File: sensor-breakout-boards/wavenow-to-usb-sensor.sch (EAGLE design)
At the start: 4 parts, among them X1 Type-A Receptacle, X2 Micro Type-B Receptacle

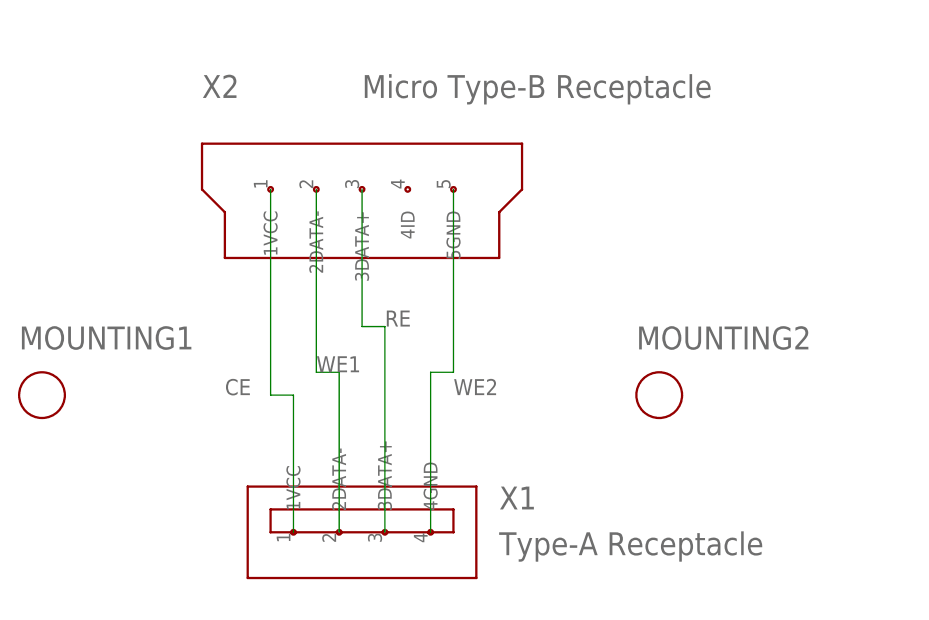
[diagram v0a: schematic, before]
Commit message: three breakout boards complete
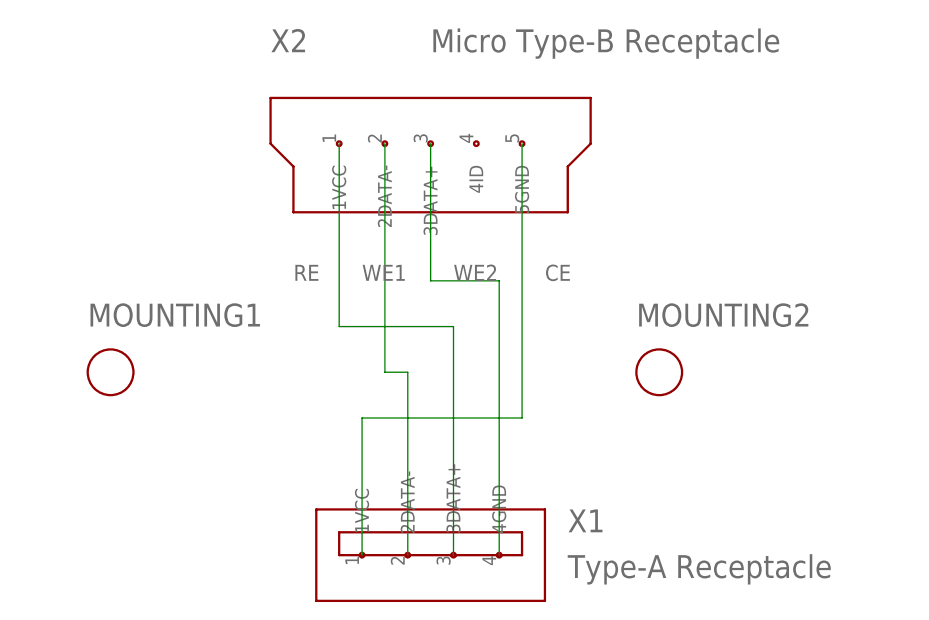
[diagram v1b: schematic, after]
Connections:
- net CE: now also X2.5GND; no longer X2.1VCC
- net RE: now also X2.1VCC; no longer X2.3DATA+
- net WE2: now also X2.3DATA+; no longer X2.5GND
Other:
- moved on the sheet: MOUNTING1, MOUNTING2, X1, X2
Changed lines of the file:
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@@
 </classes>
 <parts>
+<part name="X2" library="sensor-breakout-boards" deviceset="USB-MICRO-TYPE-B-RECEPTACLE" device="" value="Micro Type-B Receptacle"/>
 <part name="X1" library="sensor-breakout-boards" deviceset="USB-TYPE-A-RECEPTACLE" device="" value="Type-A Receptacle"/>
-<part name="X2" library="sensor-breakout-boards" deviceset="USB-MICRO-TYPE-B-RECEPTACLE" device="" value="Micro Type-B Receptacle"/>
 <part name="MOUNTING1" library="sensor-breakout-boards" deviceset="M2-MOUNTING-HOLE" device=""/>
 <part name="MOUNTING2" library="sensor-breakout-boards" deviceset="M2-MOUNTING-HOLE" device=""/>
@@
 </plain>
 <instances>
-<instance part="X1" gate="G$1" x="43.18" y="17.78"/>
-<instance part="X2" gate="G$1" x="43.18" y="55.88"/>
-<instance part="MOUNTING1" gate="G$1" x="7.62" y="33.02"/>
-<instance part="MOUNTING2" gate="G$1" x="76.2" y="33.02"/>
+<instance part="X2" gate="G$1" x="50.8" y="60.96"/>
+<instance part="X1" gate="G$1" x="50.8" y="15.24"/>
+<instance part="MOUNTING1" gate="G$1" x="15.24" y="35.56"/>
+<instance part="MOUNTING2" gate="G$1" x="76.2" y="35.56"/>
 </instances>
 <busses>
 </busses>
 <nets>
-<net name="CE" class="0">
+<net name="RE" class="0">
 <segment>
-<pinref part="X1" gate="G$1" pin="1VCC"/>
-<wire x1="35.56" y1="17.78" x2="35.56" y2="33.02" width="0.1524" layer="91"/>
-<wire x1="35.56" y1="33.02" x2="33.02" y2="33.02" width="0.1524" layer="91"/>
 <pinref part="X2" gate="G$1" pin="1VCC"/>
-<wire x1="33.02" y1="33.02" x2="33.02" y2="55.88" width="0.1524" layer="91"/>
-<label x="27.94" y="33.02" size="1.778" layer="95"/>
+<wire x1="40.64" y1="60.96" x2="40.64" y2="40.64" width="0.1524" layer="91"/>
+<pinref part="X1" gate="G$1" pin="3DATA+"/>
+<wire x1="40.64" y1="40.64" x2="53.34" y2="40.64" width="0.1524" layer="91"/>
+<wire x1="53.34" y1="40.64" x2="53.34" y2="15.24" width="0.1524" layer="91"/>
+<label x="35.56" y="45.72" size="1.778" layer="95"/>
 </segment>
 </net>
@@
 <segment>
 <pinref part="X2" gate="G$1" pin="2DATA-"/>
-<wire x1="38.1" y1="55.88" x2="38.1" y2="35.56" width="0.1524" layer="91"/>
+<wire x1="45.72" y1="60.96" x2="45.72" y2="35.56" width="0.1524" layer="91"/>
 <pinref part="X1" gate="G$1" pin="2DATA-"/>
-<wire x1="38.1" y1="35.56" x2="40.64" y2="35.56" width="0.1524" layer="91"/>
-<wire x1="40.64" y1="35.56" x2="40.64" y2="17.78" width="0.1524" layer="91"/>
-<label x="38.1" y="35.56" size="1.778" layer="95"/>
-</segment>
-</net>
-<net name="RE" class="0">
-<segment>
-<pinref part="X2" gate="G$1" pin="3DATA+"/>
-<wire x1="43.18" y1="55.88" x2="43.18" y2="40.64" width="0.1524" layer="91"/>
-<pinref part="X1" gate="G$1" pin="3DATA+"/>
-<wire x1="43.18" y1="40.64" x2="45.72" y2="40.64" width="0.1524" layer="91"/>
-<wire x1="45.72" y1="40.64" x2="45.72" y2="17.78" width="0.1524" layer="91"/>
-<label x="45.72" y="40.64" size="1.778" layer="95"/>
+<wire x1="45.72" y1="35.56" x2="48.26" y2="35.56" width="0.1524" layer="91"/>
+<wire x1="48.26" y1="35.56" x2="48.26" y2="15.24" width="0.1524" layer="91"/>
+<label x="43.18" y="45.72" size="1.778" layer="95"/>
 </segment>
 </net>
 <net name="WE2" class="0">
 <segment>
-<pinref part="X2" gate="G$1" pin="5GND"/>
-<wire x1="53.34" y1="55.88" x2="53.34" y2="35.56" width="0.1524" layer="91"/>
+<pinref part="X2" gate="G$1" pin="3DATA+"/>
+<wire x1="50.8" y1="60.96" x2="50.8" y2="45.72" width="0.1524" layer="91"/>
 <pinref part="X1" gate="G$1" pin="4GND"/>
-<wire x1="53.34" y1="35.56" x2="50.8" y2="35.56" width="0.1524" layer="91"/>
-<wire x1="50.8" y1="35.56" x2="50.8" y2="17.78" width="0.1524" layer="91"/>
-<label x="53.34" y="33.02" size="1.778" layer="95"/>
+<wire x1="50.8" y1="45.72" x2="58.42" y2="45.72" width="0.1524" layer="91"/>
+<wire x1="58.42" y1="45.72" x2="58.42" y2="15.24" width="0.1524" layer="91"/>
+<label x="53.34" y="45.72" size="1.778" layer="95"/>
 </segment>
 </net>
+<net name="CE" class="0">
+<segment>
+<pinref part="X2" gate="G$1" pin="5GND"/>
+<wire x1="60.96" y1="60.96" x2="60.96" y2="30.48" width="0.1524" layer="91"/>
+<pinref part="X1" gate="G$1" pin="1VCC"/>
+<wire x1="60.96" y1="30.48" x2="43.18" y2="30.48" width="0.1524" layer="91"/>
+<wire x1="43.18" y1="30.48" x2="43.18" y2="15.24" width="0.1524" layer="91"/>
+<label x="63.5" y="45.72" size="1.778" layer="95"/>
+</segment>
+</net>

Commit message: made changes discussed at meeting
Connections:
- net WE1: now also X1.4GND, X2.3DATA+; no longer X1.2DATA-, X2.2DATA-
- net WE2: now also X1.2DATA-, X2.2DATA-; no longer X1.4GND, X2.3DATA+
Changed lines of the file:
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@@
 </segment>
 </net>
-<net name="WE1" class="0">
+<net name="WE2" class="0">
 <segment>
 <pinref part="X2" gate="G$1" pin="2DATA-"/>
@@
 </segment>
 </net>
-<net name="WE2" class="0">
+<net name="WE1" class="0">
 <segment>
 <pinref part="X2" gate="G$1" pin="3DATA+"/>
